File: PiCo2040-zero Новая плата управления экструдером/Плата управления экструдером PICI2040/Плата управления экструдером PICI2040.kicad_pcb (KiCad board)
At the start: 2 copper layers, 100.2 x 42 mm, 32 parts, among them J10 Conn_01x08_Pin, J5 Conn_01x08_Pin, J6 Conn_01x08_Pin, J7 Conn_01x08_Pin, J8 Conn_01x08_Pin, J9 Conn_02x03_Odd_Even, Q1 IRLB8721, Q2 IRLB8721, Q3 IRLB8721, U1 rp2040-zero

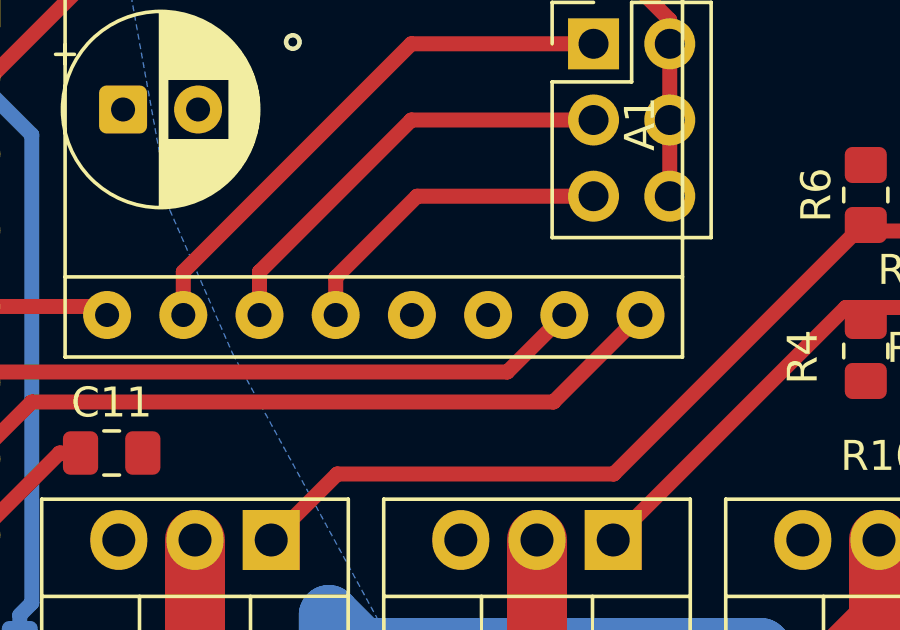
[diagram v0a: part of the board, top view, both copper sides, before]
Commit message: Правка разводки Pololu
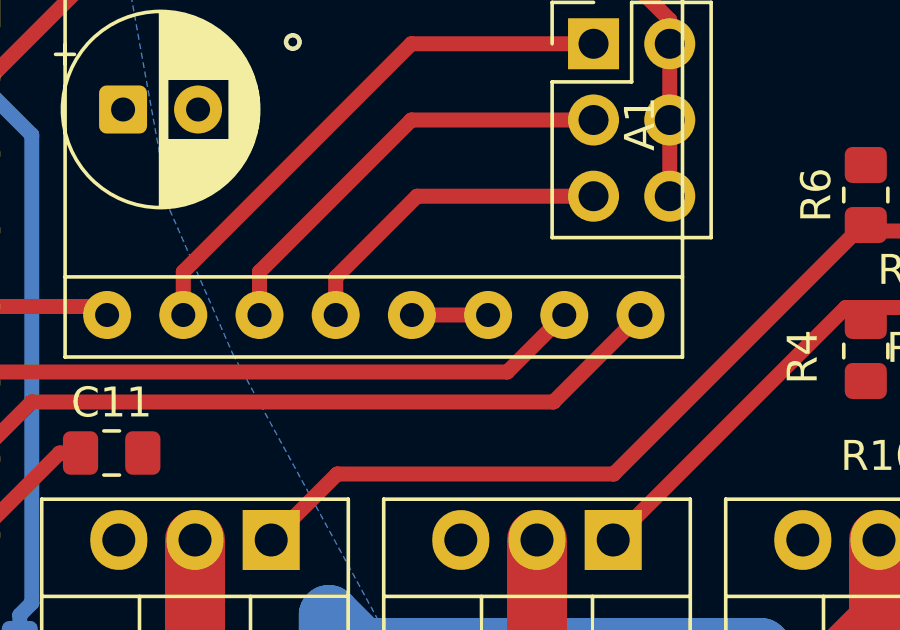
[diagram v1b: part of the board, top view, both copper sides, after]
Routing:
- net Net-(A1-~{RESET}): track 0.00 -> 2.54 mm
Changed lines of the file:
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@@
+	)
+	(segment
+		(start 120.91 100.1)
+		(end 118.37 100.1)
+		(width 0.5)
+		(layer "F.Cu")
+		(net "Net-(A1-~{RESET})")
 	)
 	(segment
